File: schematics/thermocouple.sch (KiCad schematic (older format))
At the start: 0 parts

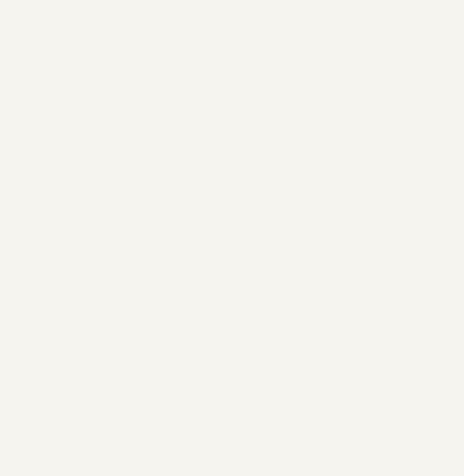
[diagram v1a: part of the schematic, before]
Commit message: Added hierarchical pins
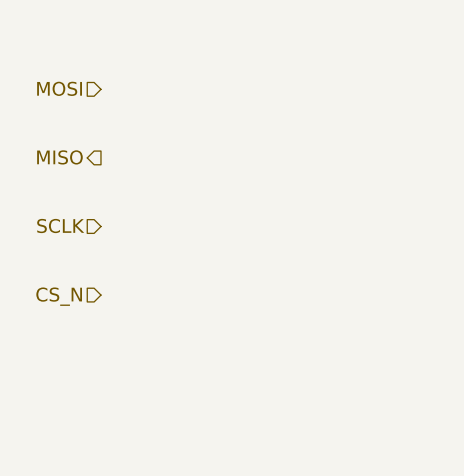
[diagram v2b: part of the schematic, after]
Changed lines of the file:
@@
-EESchema Schematic File Version 2  date Fri 04 Oct 2013 11:39:40 PM EDT
+EESchema Schematic File Version 2  date Sat 05 Oct 2013 12:10:34 AM EDT
 LIBS:power
 LIBS:device
@@
 Comment4 ""
 $EndDescr
+Text HLabel 1550 2850 0    60   Input ~ 0
+CS_N
+Text HLabel 1550 2550 0    60   Input ~ 0
+SCLK
+Text HLabel 1550 2250 0    60   Output ~ 0
+MISO
+Text HLabel 1550 1950 0    60   Input ~ 0
+MOSI
 Text HLabel 9150 2050 2    60   Input ~ 0
 TC_in-
